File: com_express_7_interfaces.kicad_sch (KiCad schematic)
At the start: 8 parts, among them J12 Plug_Bus_CE7_EPT_401-51501-51

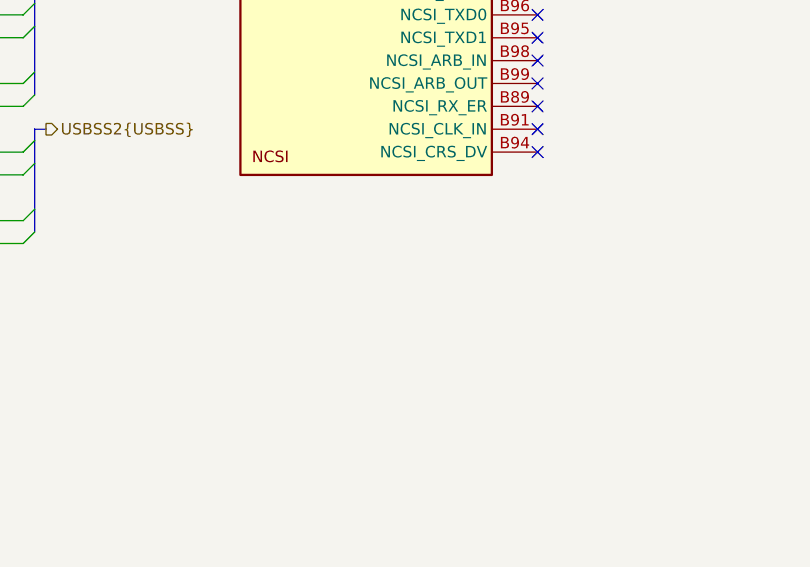
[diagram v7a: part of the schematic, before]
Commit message: Add Mech_SolidRun_LX2160A-CEX7 to schematic
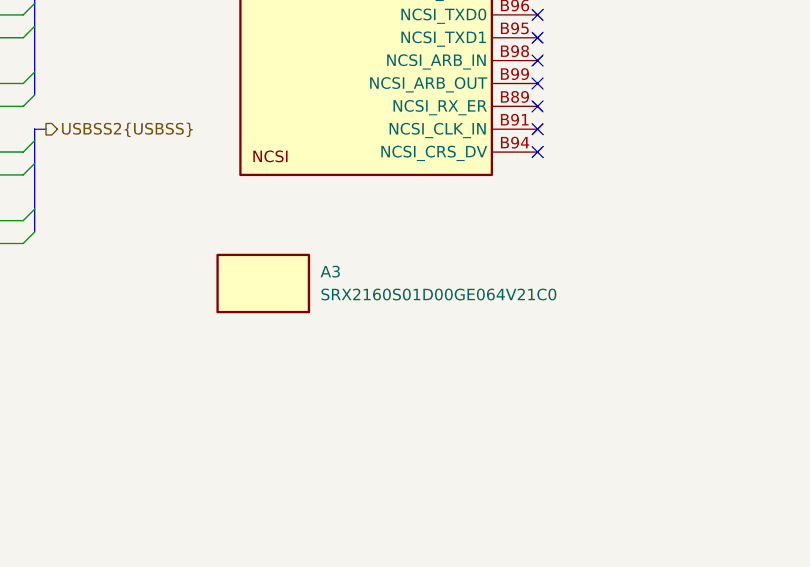
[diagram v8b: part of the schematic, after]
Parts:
- added A3: Mech_SolidRun_LX2160A-CEX7, antmicro-footprints:Mech_SolidRun_LX2160A-CEX7, symbol antmicroModules:Mech_SolidRun_LX2160A-CEX7
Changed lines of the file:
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@@
+    )
+  )
+  (symbol (lib_id "antmicroModules:Mech_SolidRun_LX2160A-CEX7") (at 246.38 232.41 0) (unit 1)
+    (in_bom no) (on_board yes) (dnp no) (fields_autoplaced)
+    (property "Reference" "A3" (at 257.81 234.315 0)
+      (effects (font (size 1.27 1.27) (thickness 0.15)) (justify left))
+    )
+    (property "Value" "Mech_SolidRun_LX2160A-CEX7" (at 260.35 236.22 0)
+      (effects (font (size 1.27 1.27) (thickness 0.15)) (justify left bottom) hide)
+    )
+    (property "Footprint" "antmicro-footprints:Mech_SolidRun_LX2160A-CEX7" (at 260.35 238.76 0)
+      (effects (font (size 1.27 1.27) (thickness 0.15)) (justify left bottom) hide)
+    )
+    (property "Datasheet" "https://www.solid-run.com/embedded-networking/nxp-lx2160a-family/cex7-lx2160/#documentation" (at 260.35 241.3 0)
+      (effects (font (size 1.27 1.27) (thickness 0.15)) (justify left bottom) hide)
+    )
+    (property "MPN" "SRX2160S01D00GE064V21C0" (at 257.81 236.855 0)
+      (effects (font (size 1.27 1.27) (thickness 0.15)) (justify left))
+    )
+    (property "Manufacturer" "SolidRun" (at 260.35 246.38 0)
+      (effects (font (size 1.27 1.27) (thickness 0.15)) (justify left bottom) hide)
+    )
+    (property "Author" "Antmicro" (at 260.35 248.92 0)
+      (effects (font (size 1.27 1.27) (thickness 0.15)) (justify left bottom) hide)
+    )
+    (property "License" "Apache-2.0" (at 260.35 251.46 0)
+      (effects (font (size 1.27 1.27) (thickness 0.15)) (justify left bottom) hide)
+    )
+    (instances
+      (project "com-express-7-baseboard"
+        (path "/1b8c34da-dad5-4b0b-8c4b-45db766c4dfa/d0206463-9f0a-4ce9-a6c7-202004597ed5"
+          (reference "A3") (unit 1)
+        )
+      )
     )
   )
